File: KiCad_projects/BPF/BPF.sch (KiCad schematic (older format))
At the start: 107 parts, among them J1 Barrel_Jack, J2 POWER, P10 CONN_01X01, P2 ANT/PA, P3 TRX, P5 CONN_01X06, P7 CONN_01X01, P8 CONN_01X01, P9 CONN_01X01, U1 74LS145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

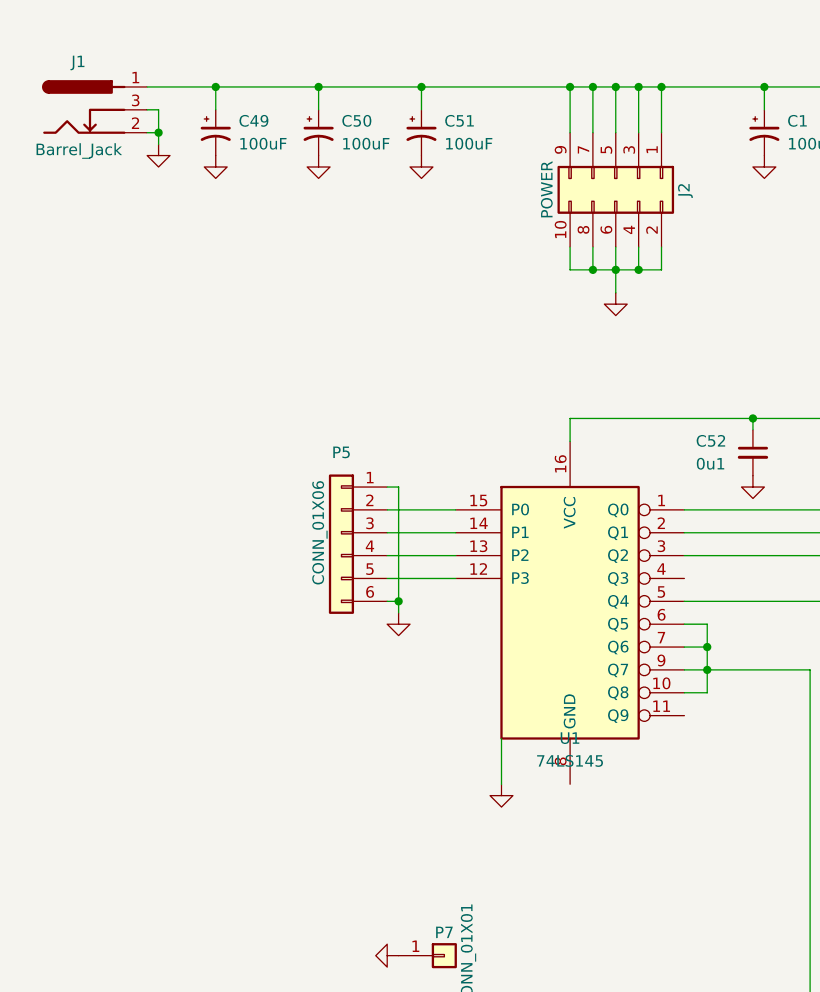
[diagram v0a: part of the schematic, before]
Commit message: Fix Issues with PCB Silk Text
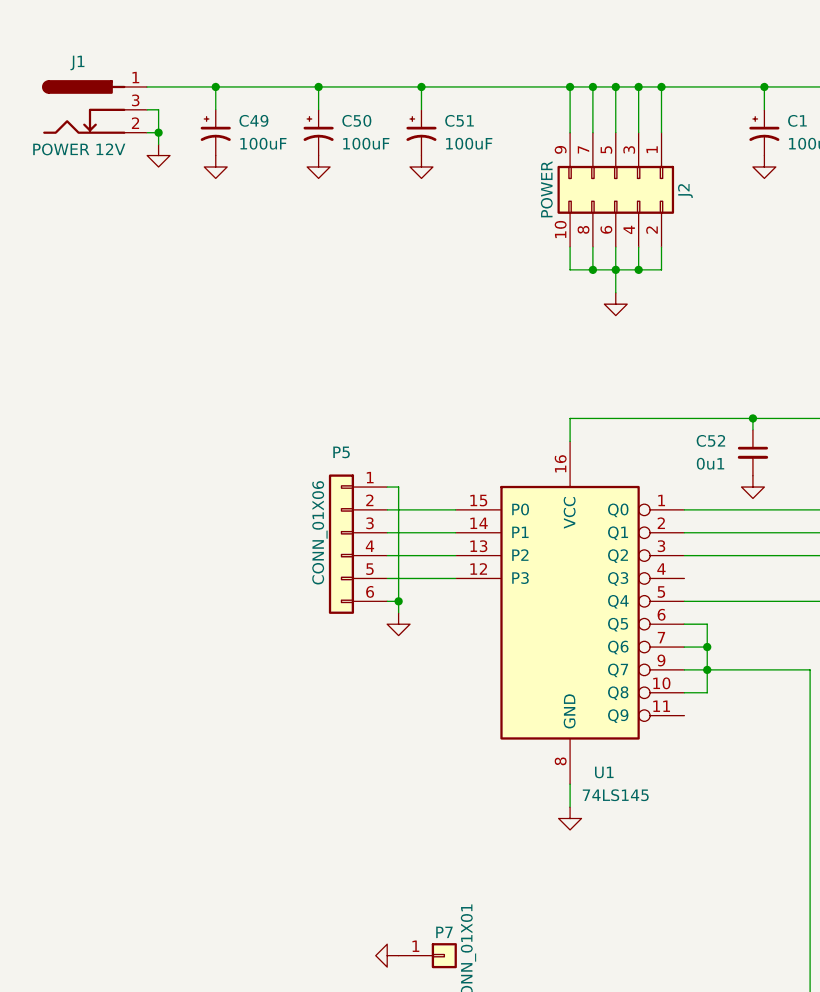
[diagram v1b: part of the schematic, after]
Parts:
- J1: value Barrel_Jack -> POWER 12V
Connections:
- net GND: now also U1.8 (GND)
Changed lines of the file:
@@
 encoding utf-8
 Sheet 1 1
-Title "BPF UT3MK"
+Title "BPF US5NCJ"
 Date "2018-01-01"
-Rev "1.04"
+Rev "1.05"
 Comp "Vasyl Kuzmenko"
 Comment1 ""
@@
 U 1 1 586EC023
 P 3100 3050
-F 0 "U1" H 3100 2450 50  0000 C CNN
-F 1 "74LS145" H 3100 2350 50  0000 C CNN
+F 0 "U1" H 3250 2300 50  0000 C CNN
+F 1 "74LS145" H 3300 2200 50  0000 C CNN
 F 2 "Housings_SOIC:SOIC-16_3.9x9.9mm_Pitch1.27mm" H 3100 3050 50  0001 C CNN
 F 3 "" H 3100 3050 50  0000 C CNN
@@
 L GND #PWR032
 U 1 1 586EF97E
-P 2800 3850
-F 0 "#PWR032" H 2800 3600 50  0001 C CNN
-F 1 "GND" H 2800 3700 50  0001 C CNN
-F 2 "" H 2800 3850 50  0000 C CNN
-F 3 "" H 2800 3850 50  0000 C CNN
-	1    2800 3850
-	1    0    0    -1
-$EndComp
-Wire Wire Line
-	2800 3850 2800 3650
+P 3100 3950
+F 0 "#PWR032" H 3100 3700 50  0001 C CNN
+F 1 "GND" H 3100 3800 50  0001 C CNN
+F 2 "" H 3100 3950 50  0000 C CNN
+F 3 "" H 3100 3950 50  0000 C CNN
+	1    3100 3950
+	1    0    0    -1
+$EndComp
 $Comp
 L Conn_01x06 P5
@@
 P 950 900
 F 0 "J1" H 950 1110 50  0000 C CNN
-F 1 "Barrel_Jack" H 950 725 50  0000 C CNN
+F 1 "POWER 12V" H 950 725 50  0000 C CNN
 F 2 "Connect:BARREL_JACK" H 1000 860 50  0001 C CNN
 F 3 "" H 1000 860 50  0001 C CNN
@@
 	1    0    0    -1
 $EndComp
+Wire Wire Line
+	3100 3850 3100 3950
 $EndSCHEMATC
